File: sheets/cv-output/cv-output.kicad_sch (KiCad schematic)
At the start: 4 parts, among them U1 TL071

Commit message: Verify cv-output against the TL07x datasheet
TI SLOS080 gives output short-circuit duration as continuous, so the TL071 protects its own output. R1 therefore stays at 1k, for capacitive isolation and to limit current into the clamps, rather than being sized to save the part.

This is the opposite conclusion to gate-output, where a CMOS pin has a hard plus or minus 10mA limit and no internal limiting, so 2k2 is required. Copying 2k2 here would have doubled the CV output impedance for no gain. The README says so explicitly.

Also records what the datasheet says about swing: roughly plus or minus 10V on a plus or minus 12V supply, not 12, because a TL07x does not reach its rails. And that CV_IN has no protection and must not face a jack, since the input pins share the same plus or minus 10mA limit and the common-mode range stops 1.5V above the negative rail.

U1 renamed to TL071CP to match the MPN naming convention.
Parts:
- U1: symbol Eurorack Common:TL071 -> Eurorack Common:TL071CP
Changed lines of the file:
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@@
 )
   (symbol
-    (lib_id "Eurorack Common:TL071")
+    (lib_id "Eurorack Common:TL071CP")
     (at 114.3 88.9 0)
     (unit 1)

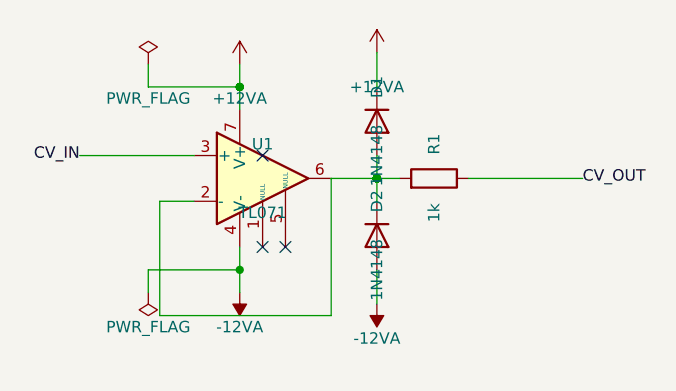
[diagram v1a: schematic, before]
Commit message: Tidy block schematic layouts
Visual changes only, made in Eeschema. ERC unchanged: 0 errors on power-input, gate-output and cv-output.
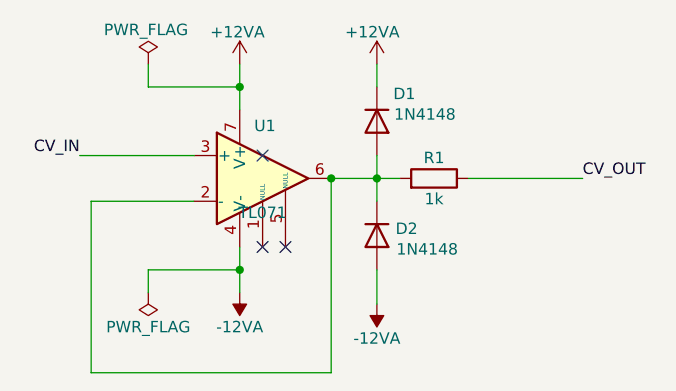
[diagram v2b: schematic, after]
